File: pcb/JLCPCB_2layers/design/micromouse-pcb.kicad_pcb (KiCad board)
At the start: 2 copper layers, 100 x 120 mm, 139 parts, among them J1 JST_XH_B2B-XH-A_1x02_P2.50mm_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, J10 AMASS_XT60-M_1x02_P7.20mm_Ver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, J5 JST_ZH_B6B-ZR_1x06_P1.50mm_Ve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, J6 JST_ZH_B6B-ZR_1x06_P1.50mm_Ve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, J7 USB_C_Receptacle_GCT_USB4105-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, J9 JST_XH_B3B-XH-A_1x03_P2.50mm_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, Q1 SOT-23, Q16 SOT-23, Q17 SOT-23, Q18 SOT-23, Q2 LED_D5.0mm_IRBlack, Q28 SOT-23, Q29 SOT-23, Q3 LED_D5.0mm_IRBlack, Q30 SOT-23, Q31 SOT-23, Q32 SOT-23, Q33 SOT-23, Q34 SOT-23, Q4 LED_D5.0mm_IRBlack, Q5 LED_D5.0mm_IRBlack, Q6 LED_D5.0mm_IRBlack, Q7 LED_D5.0mm_IRBlack, SW1 SW_PUSH_6mm, SW2 SW_PUSH_6mm, SW3 SW_PUSH_6mm, SW4 SW_PUSH_6mm, SW5 SW_SPDT_PCM12, SW6 SW_SPDT_PCM12, U1 TSOT-23-6, U2 SSOP-24_5.3x8.2mm_P0.65mm, U3 ESP32-S3-WROOM-1, U6 SOT-23-6, U7 SOT-23-6, U8 VAL

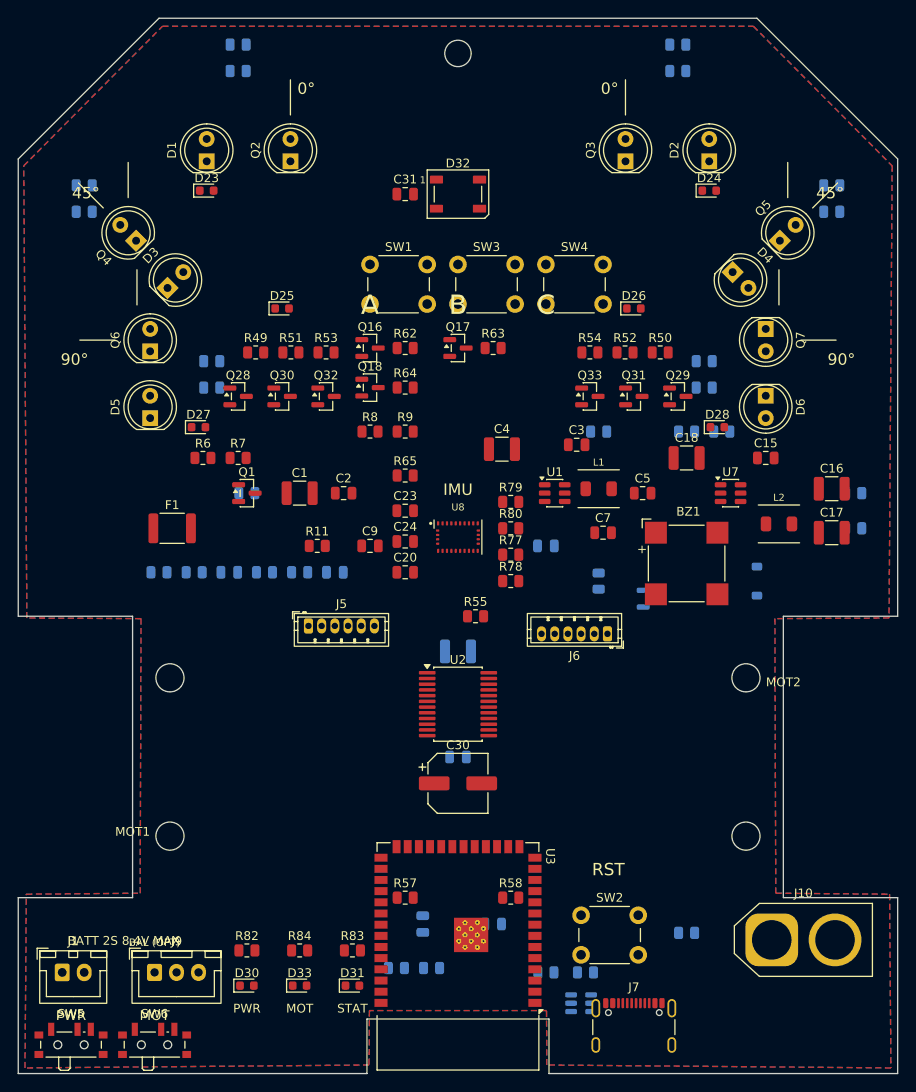
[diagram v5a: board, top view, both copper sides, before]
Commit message: 2-layer: board ROUTED via Freerouting (score 994, 1187 tracks); parity 0
Routing pipeline (the project's documented primary path): clean placement ->
export_dsn -> Freerouting 2.2.4 headless -> import_ses. 207 nets routed,
final score 994.61, 1187 track segments + 138 routed vias + 174 clearance-
checked GND stitch vias. sync_board_meta -> schematic parity 0/0.

Finalization pending (documented): 1 copper_edge_clearance (BATT_RAW runs
0.18mm from the antenna-notch edge in the congested rear -- needs a local
reroute below J7/U6, not a nudge) + 22 GND pour fragments needing connection
+ silk refdes->fab (finalize.py, after ratsnest 0).

Co-Authored-By: Claude Fable 5 <noreply@anthropic.com>
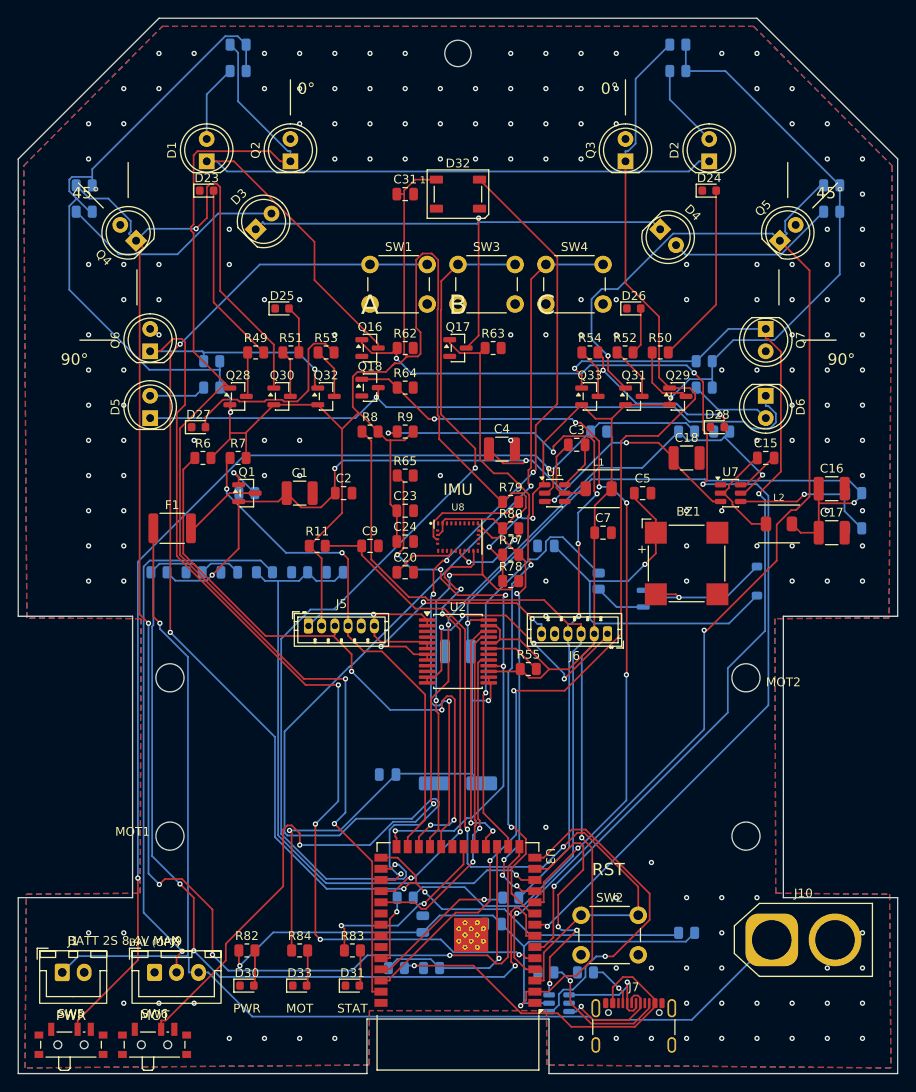
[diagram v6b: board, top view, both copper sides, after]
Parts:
- BZ1: value MagneticBuzzer_CUI_CMT-8504-100-SMT -> CMT-8504-100-SMT (magnetic transducer 8.5mm, 15R coil, 4kHz; pads 3/4 are mechanical dummies); footprint MagneticBuzzer_CUI_CMT-8504-100-SMT -> Buzzer_Beeper:MagneticBuzzer_CUI_CMT-8504-100-SMT
- C1, C11, C16, C17, C18, C4: footprint C_1210_3225Metric -> Capacitor_SMD:C_1210_3225Metric
- C10: value C_0805_2012Metric -> 10uF; footprint C_0805_2012Metric -> Capacitor_SMD:C_0805_2012Metric
- C12, C14, C15, C2, C24, C3, C5, C7: footprint C_0805_2012Metric -> Capacitor_SMD:C_0805_2012Metric
- C19, C20, C23, C31, C6, C8: value C_0805_2012Metric -> 100nF; footprint C_0805_2012Metric -> Capacitor_SMD:C_0805_2012Metric
- C30: footprint CP_Elec_6.3x7.7 -> Capacitor_SMD:CP_Elec_6.3x7.7; moved to B.Cu
- C9: value C_0805_2012Metric -> 1uF; footprint C_0805_2012Metric -> Capacitor_SMD:C_0805_2012Metric
- D1, D2, D3, D4, D5, D6: value LED_D5.0mm_IRGrey -> IR333-A (Everlight 5mm 940nm 20deg; LD271 base symbol; TSAL6400 is lifecycle-Obsolete at Lion); footprint LED_D5.0mm_IRGrey -> LED_THT:LED_D5.0mm_IRGrey
- D23, D24, D25, D26, D27, D28: value LED_0603_1608Metric -> Indicator LED 0603 super-red AlInGaP, high-eff bin (e.g. APT1608SURCK); footprint LED_0603_1608Metric -> LED_SMD:LED_0603_1608Metric
- D29: value D_SOD-123 -> 1N4148W (flyback clamp across the buzzer coil); footprint D_SOD-123 -> Diode_SMD:D_SOD-123
- D30: value LED_0603_1608Metric -> Power LED 0603 green (JLC good-stock); footprint LED_0603_1608Metric -> LED_SMD:LED_0603_1608Metric
- D31: value LED_0603_1608Metric -> Status LED 0603 blue (JLC good-stock); footprint LED_0603_1608Metric -> LED_SMD:LED_0603_1608Metric
- D32: value LED_WS2812B_PLCC4_5.0x5.0mm_P3.2mm -> WS2812B addressable RGB 5050 (JLC good-stock); footprint LED_WS2812B_PLCC4_5.0x5.0mm_P3.2mm -> LED_SMD:LED_WS2812B_PLCC4_5.0x5.0mm_P3.2mm
- D33: value LED_0603_1608Metric -> Motor-power LED 0603 (VM_6V present; JLC good-stock); footprint LED_0603_1608Metric -> LED_SMD:LED_0603_1608Metric
- F1: value Fuse_1812_4532Metric -> 2.6A/16V PPTC; footprint Fuse_1812_4532Metric -> Fuse:Fuse_1812_4532Metric
- J1: value JST_XH_B2B-XH-A_1x02_P2.50mm_Vertical -> BATT_IN_2S; footprint JST_XH_B2B-XH-A_1x02_P2.50mm_Vertical -> Connector_JST:JST_XH_B2B-XH-A_1x02_P2.50mm_Vertical
- J10: value AMASS_XT60-M_1x02_P7.20mm_Vertical -> BATT_IN_XT60 (parallel option -- ONE PACK ONLY); footprint AMASS_XT60-M_1x02_P7.20mm_Vertical -> Connector_AMASS:AMASS_XT60-M_1x02_P7.20mm_Vertical
- J5: value JST_ZH_B6B-ZR_1x06_P1.50mm_Vertical -> MOTOR_A_N20_ENCODER; footprint JST_ZH_B6B-ZR_1x06_P1.50mm_Vertical -> Connector_JST:JST_ZH_B6B-ZR_1x06_P1.50mm_Vertical
- J6: value JST_ZH_B6B-ZR_1x06_P1.50mm_Vertical -> MOTOR_B_N20_ENCODER; footprint JST_ZH_B6B-ZR_1x06_P1.50mm_Vertical -> Connector_JST:JST_ZH_B6B-ZR_1x06_P1.50mm_Vertical
- J7: value USB_C_Receptacle_GCT_USB4105-xx-A_16P_TopMnt_Horizontal -> USB-C rear (GCT USB4105; VBUS unused -- battery powers the board); footprint USB_C_Receptacle_GCT_USB4105-xx-A_16P_TopMnt_Horizontal -> Connector_USB:USB_C_Receptacle_GCT_USB4105-xx-A_16P_TopMnt_Horizontal
- J9: value JST_XH_B3B-XH-A_1x03_P2.50mm_Vertical -> BALANCE_2S; footprint JST_XH_B3B-XH-A_1x03_P2.50mm_Vertical -> Connector_JST:JST_XH_B3B-XH-A_1x03_P2.50mm_Vertical
- L1, L2: footprint L_Bourns_SRP4020TA -> n20:L_Bourns_SRP4020TA
- Q1: value SOT-23 -> Q_PMOS reverse guard (DMP3098L-7: Vgs +/-20V, 2S-safe); footprint SOT-23 -> Package_TO_SOT_SMD:SOT-23
- Q16, Q17, Q18: value SOT-23 -> BSS138 (real part; Q_NMOS_GSD base symbol used so ERC checks pins); footprint SOT-23 -> Package_TO_SOT_SMD:SOT-23
- Q2, Q3, Q4, Q5, Q6, Q7: value LED_D5.0mm_IRBlack -> PT334-6B (5mm filtered PT; LONG LEAD = EMITTER; SFH309 base symbol so ERC checks pins); footprint LED_D5.0mm_IRBlack -> LED_THT:LED_D5.0mm_IRBlack
- Q28, Q29, Q30, Q31, Q32, Q33: value SOT-23 -> BSS84 (PMOS indicator driver; Q_PMOS base symbol); footprint SOT-23 -> Package_TO_SOT_SMD:SOT-23
- Q34: value SOT-23 -> MMBT2222A (buzzer low-side driver; Q_NPN_BEC base symbol so ERC checks pins); footprint SOT-23 -> Package_TO_SOT_SMD:SOT-23
- R1, R2, R62, R63, R64, R69, R73, R75, R76: value R_0805_2012Metric -> 100k; footprint R_0805_2012Metric -> Resistor_SMD:R_0805_2012Metric
- R10, R11, R55, R6, R65, R67, R7, R79, R8, R80, R9: value R_0805_2012Metric -> 10k; footprint R_0805_2012Metric -> Resistor_SMD:R_0805_2012Metric
- R12, R56: value R_0805_2012Metric -> 5.1k; footprint R_0805_2012Metric -> Resistor_SMD:R_0805_2012Metric
- R13, R15, R17, R19, R21, R23: value R_0805_2012Metric -> 47k; footprint R_0805_2012Metric -> Resistor_SMD:R_0805_2012Metric
- R14, R16, R18, R20, R22, R24: value R_0805_2012Metric -> 33; footprint R_0805_2012Metric -> Resistor_SMD:R_0805_2012Metric
- R3: value R_0805_2012Metric -> 39k; footprint R_0805_2012Metric -> Resistor_SMD:R_0805_2012Metric
- R49, R50, R51, R52, R53, R54, R82, R83, R84: value R_0805_2012Metric -> 1k; footprint R_0805_2012Metric -> Resistor_SMD:R_0805_2012Metric
- R57, R58: value R_0805_2012Metric -> 1k; footprint R_0805_2012Metric -> Resistor_SMD:R_0805_2012Metric; moved to B.Cu
- R68: value R_0805_2012Metric -> 15k; footprint R_0805_2012Metric -> Resistor_SMD:R_0805_2012Metric
- R70: value R_0805_2012Metric -> 220k; footprint R_0805_2012Metric -> Resistor_SMD:R_0805_2012Metric
- R71: value R_0805_2012Metric -> 110k; footprint R_0805_2012Metric -> Resistor_SMD:R_0805_2012Metric
- R74: value R_0805_2012Metric -> 11k; footprint R_0805_2012Metric -> Resistor_SMD:R_0805_2012Metric
- R77, R78: value R_0805_2012Metric -> 4.7k; footprint R_0805_2012Metric -> Resistor_SMD:R_0805_2012Metric
- R81: value R_0805_2012Metric -> 220; footprint R_0805_2012Metric -> Resistor_SMD:R_0805_2012Metric
- SW1: value SW_PUSH_6mm -> BTN_A (start / BOOT); footprint SW_PUSH_6mm -> Button_Switch_THT:SW_PUSH_6mm
- SW2: value SW_PUSH_6mm -> RESET; footprint SW_PUSH_6mm -> Button_Switch_THT:SW_PUSH_6mm
- SW3: value SW_PUSH_6mm -> BTN_B; footprint SW_PUSH_6mm -> Button_Switch_THT:SW_PUSH_6mm
- SW4: value SW_PUSH_6mm -> BTN_C; footprint SW_PUSH_6mm -> Button_Switch_THT:SW_PUSH_6mm
- SW5: value SW_SPDT_PCM12 -> PWR ALL (PCM12SMTR slide; slide-to-GND = OFF); footprint SW_SPDT_PCM12 -> Button_Switch_SMD:SW_SPDT_PCM12
- SW6: value SW_SPDT_PCM12 -> PWR MOTORS (PCM12SMTR slide; slide-to-GND = motors OFF); footprint SW_SPDT_PCM12 -> Button_Switch_SMD:SW_SPDT_PCM12
- U1: value TSOT-23-6 -> AP63203WU-7 (fixed 3.3V 2A buck; AP63200WU base symbol so ERC checks pins); footprint TSOT-23-6 -> Package_TO_SOT_SMD:TSOT-23-6
- U2: value SSOP-24_5.3x8.2mm_P0.65mm -> TB6612FNG; footprint SSOP-24_5.3x8.2mm_P0.65mm -> Package_SO:SSOP-24_5.3x8.2mm_P0.65mm
- U3: value ESP32-S3-WROOM-1 -> ESP32-S3-WROOM-1-N8R2 (quad PSRAM: IO35-37 usable; octal -R8 would lose them); footprint ESP32-S3-WROOM-1 -> RF_Module:ESP32-S3-WROOM-1
- U6: value SOT-23-6 -> USBLC6-2SC6 (SOT-23-6; 2P6 base symbol so ERC checks pins); footprint SOT-23-6 -> Package_TO_SOT_SMD:SOT-23-6
- U7: value SOT-23-6 -> TPS54302DDCR (6.0V/3A motor buck; FB=100k/11k); footprint SOT-23-6 -> Package_TO_SOT_SMD:SOT-23-6
- U8: value VAL -> BNO055 (9-axis IMU + fusion; 3.3V native; I2C 0x28); footprint BNO055 -> n20:BNO055
- moved D3 12.0 mm to (27.0, 24.0)
- moved D4 9.57 mm to (73.0, 24.0)
- moved R55 8.49 mm to (58.0, 74.0)
- moved C12 8.25 mm to (42.0, 86.0)
- moved U2 6.00 mm to (50.0, 72.0)
- moved U6 2.50 mm to (61.5, 112.0)
- turned C30 to 180 degrees
- turned R57 to 180 degrees
- turned R58 to 180 degrees
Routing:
- net PLUS3V3: track 0.00 -> 564.8 mm, vias 0 -> 9
- net WALL3_SENSE: track 0.00 -> 186.7 mm, vias 0 -> 5
- net USER_BTN: track 0.00 -> 150.1 mm, vias 0 -> 4
- net WALL4_SENSE: track 0.00 -> 145.8 mm, vias 0 -> 3
- net WALL1_SENSE: track 0.00 -> 141.5 mm, vias 0 -> 2
- net BATT_RAW: track 0.00 -> 139.5 mm, vias 0 -> 1
- net WALL2_SENSE: track 0.00 -> 135.9 mm, vias 0 -> 2
- net WALL5_SENSE: track 0.00 -> 132.2 mm, vias 0 -> 5
- net PWR_EN: track 0.00 -> 131.1 mm, vias 0 -> 2
- net VM_6V: track 0.00 -> 130.9 mm, vias 0 -> 4
- net WALL_EMIT_FRONT: track 0.00 -> 123.8 mm, vias 0 -> 4
- net MOT_EN: track 0.00 -> 122.9 mm, vias 0 -> 4
- net USER_BTN3: track 0.00 -> 118.8 mm, vias 0 -> 2
- net WALL6_SENSE: track 0.00 -> 110.1 mm, vias 0 -> 3
- net VBAT_SENSE: track 0.00 -> 106.9 mm, vias 0 -> 3
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
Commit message: 2-layer: debug tooling crashes + crash-isolated GND heal (22->16 ratsnest)
Root-caused the crashes:
- Segfaults = non-deterministic SWIG heap corruption from accumulating many
  pcbnew mutations (Remove/fill) in ONE process (dangling wrapper objects).
  Fix: crash-isolation -- one small batch per process, save + os._exit(0)
  (skip the crashy SWIG cleanup), reload fresh next batch.
- OOM/timeouts = in-house A* with 600k-2M expansion budgets on congested
  2-layer nets. Fix: cap budgets to 300k (fail-fast).

Applied: heal_all crash-isolated (bridge_fragments maxn cap, smallest-first,
capped A*, __main__ guard) + a bash driver loop. Healed GND 22->16, clean
(no new errors, parity 0). Remaining 16 are doubly-walled in the dense IMU/
centre region (both copper layers blocked) -- heal_all's hard floor.

Freerouting-GND-routable fully routes GND (score 994, 0 unrouted) but won't
write its SES on that net -- deterministic Freerouting bug (3 attempts incl
6GB heap; not an OOM). 1 BATT_RAW edge-clearance + 16 GND fragments remain;
they need the GUI push-shove router to move signal tracks and open GND paths.

Co-Authored-By: Claude Fable 5 <noreply@anthropic.com>
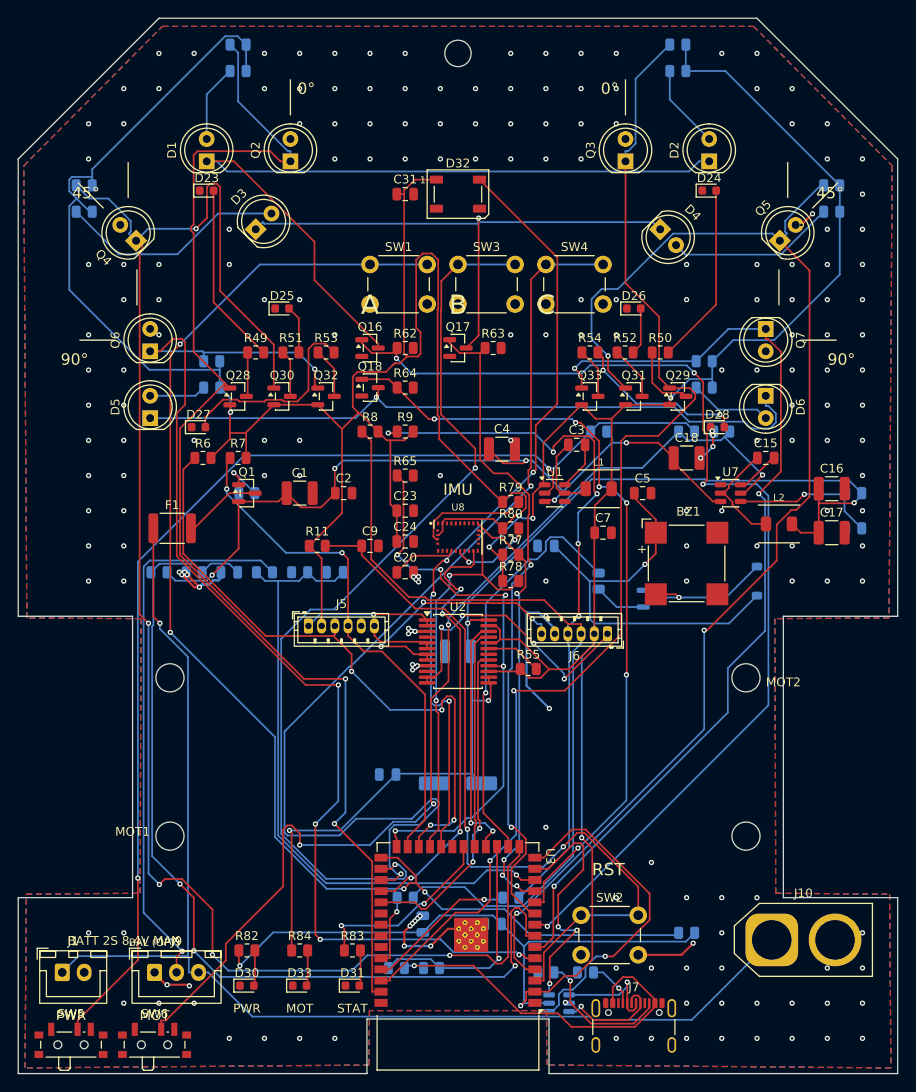
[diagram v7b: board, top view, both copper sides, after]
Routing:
- net GND: track 0.00 -> 68.7 mm, vias 174 -> 209

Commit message: 2-layer: user placement review + motor-bay routing + full route (0 err / 0 parity)
Extensive user-directed placement/mechanical review, then routed to a
manufacturable state:

Placement (user render review):
- Diagonal IR emitters D3/D4 restored to the 45-deg cluster + detectors Q4/Q5
  rotated to align (reverts the 1297b67 center-pull); shifted up 2mm to clear
  the side detectors within the front edge-gap.
- Obstruction sensor pull-ups R13-R20 moved behind/inboard of their sensors,
  off the beam path.
- C30 (6.3x7.7mm electrolytic) moved OFF the bottom layer -> TOP by R6/R7:
  a 7.7mm part on the bottom would drag on the maze floor. Bottom is now all
  low-profile SMD. Kept clear of the motor + mount.
- J6 made mirror-symmetric to J5 (rot 180) so it clears the H3 mount hole.
- BATT label moved to the battery connectors; PWR/MOT switch labels lifted off
  the switch bodies (were unreadable).

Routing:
- USER insight: opened the motor-bay TOP space (the F.Cu motor keepout blocked
  Freerouting from the top under the motors). Motors have no copper pads and sit
  on standoffs, so top routing + top GND pour there are fine. MOT1 now 19 / MOT2
  16 top tracks; top pour fills the bays -> less GND fragmentation.
- Hard U3-escape nets pre-routed on the empty board; Freerouting completes 100%
  of signal (0 unrouted, score 994.80).
- GND pour stitched with vias (smart + chained, deduped) to ratsnest 5. The
  remaining 5 are non-critical: 2 redundant IMU (BNO055) ground pads (the IMU is
  grounded via its 4 other GND pads) + 3 floating pour slivers. Every critical
  ground connects.

Verify: 0 DRC errors, 0 schematic parity, silk finalized (refdes -> fab),
check_pins 28/28, ERC 0. Renders refreshed (top + bottom, placement + routed).

Co-Authored-By: Claude Opus 4.8 (1M context) <noreply@anthropic.com>
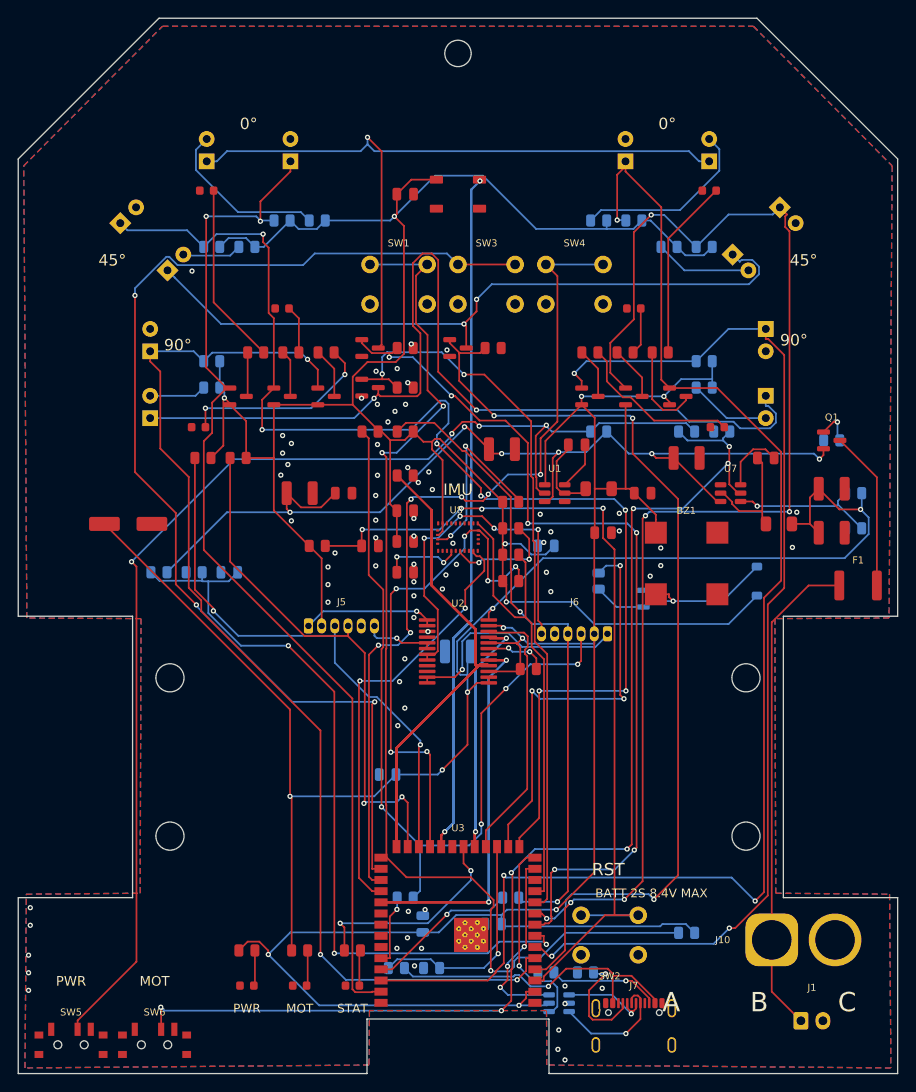
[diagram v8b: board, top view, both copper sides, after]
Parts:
- removed C19: 100nF, Capacitor_SMD:C_0805_2012Metric
- removed J9: BALANCE_2S, Connector_JST:JST_XH_B3B-XH-A_1x03_P2.50mm_Vertical
- removed R75, R76: 100k, Resistor_SMD:R_0805_2012Metric
- C30: moved to F.Cu
- moved J1 84.2 mm to (89.0, 114.0)
- moved F1 78.3 mm to (95.5, 64.5)
- moved Q1 66.8 mm to (92.5, 48.0)
- moved R1 66.8 mm to (92.5, 48.0)
- moved C30 47.7 mm to (12.5, 57.5), turned to 0 degrees
- moved R13 20.6 mm to (30.0, 23.0)
- moved R15 20.6 mm to (70.0, 23.0)
- moved R14 19.2 mm to (34.0, 23.0)
- moved R16 19.2 mm to (66.0, 23.0)
- moved R18 18.9 mm to (26.0, 26.0)
- moved R20 18.9 mm to (74.0, 26.0)
- moved R17 16.1 mm to (22.0, 26.0)
- moved R19 16.1 mm to (78.0, 26.0)
- moved D3 11.1 mm to (17.0, 28.7)
- moved D4 8.72 mm to (81.2, 26.9)
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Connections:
- U3 pad 12: BAT_MID_SENSE -> unconnected-(U3-IO8-Pad12)
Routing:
- net RGB_DATA: track 88.7 -> 200.9 mm, vias 4 -> 2
- net BIN2: track 64.2 -> 153.2 mm, vias 5 -> 0
- net BATT_RAW: track 139.5 -> 56.1 mm, vias 1 -> 0
- net BAT_MID_SENSE: track 72.9 -> 0.00 mm, vias 1 -> 0
- net PLUS3V3: track 564.8 -> 493.1 mm, vias 9 -> 11
- net GND: track 68.7 -> 0.00 mm, vias 209 -> 76
- net BAT_MID: track 63.7 -> 0.00 mm, vias 1 -> 0
- net BIN1: track 37.4 -> 82.3 mm
- net WALL3_SENSE: track 186.7 -> 143.3 mm, vias 5 -> 7
- net VM_6V: track 130.9 -> 171.0 mm, vias 4 -> 5
- net EMIT_SIDE_K: track 78.8 -> 109.4 mm, vias 1 -> 2
- net WALL_EMIT_DIAG: track 76.4 -> 103.4 mm, vias 2 -> 4
- net USER_BTN2: track 104.7 -> 130.1 mm, vias 2 -> 3
- net WALL1_SENSE: track 141.5 -> 116.9 mm
- net AIN1: track 25.1 -> 49.2 mm, vias 0 -> 2
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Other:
- board text removed: "BAL (OPT)"
